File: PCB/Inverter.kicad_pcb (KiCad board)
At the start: 2 copper layers, 71.4 x 98.7 mm, 79 parts, among them J1 Conn_01x02, J2 Conn_01x05_Pin, J3 Conn_01x05_Pin, Q1 STP110N8F6, Q2 STP110N8F6, Q3 STP110N8F6, Q4 STP110N8F6, Q5 STP110N8F6, Q6 STP110N8F6, U1 XL7015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

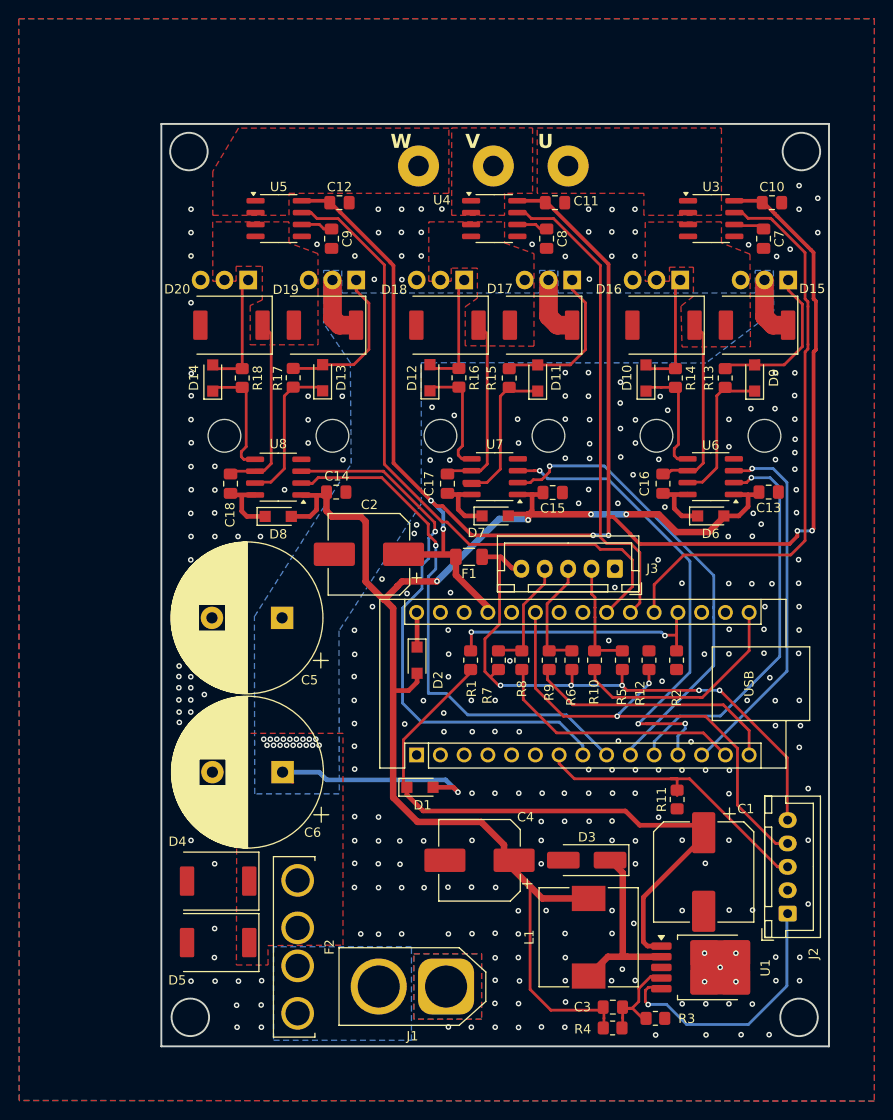
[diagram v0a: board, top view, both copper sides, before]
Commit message: Change#009
Changed the pin on phase W from 5 to 3 (so that all PWMs are at the same frequency);
Added a thermal barrier for all components on the negative side to make it easier to assemble the device;
Changed the size of the board, it became a little larger (to increase the ground current);
Added frames for connectors with a description in the diagram for a better understanding of which connector is for what.
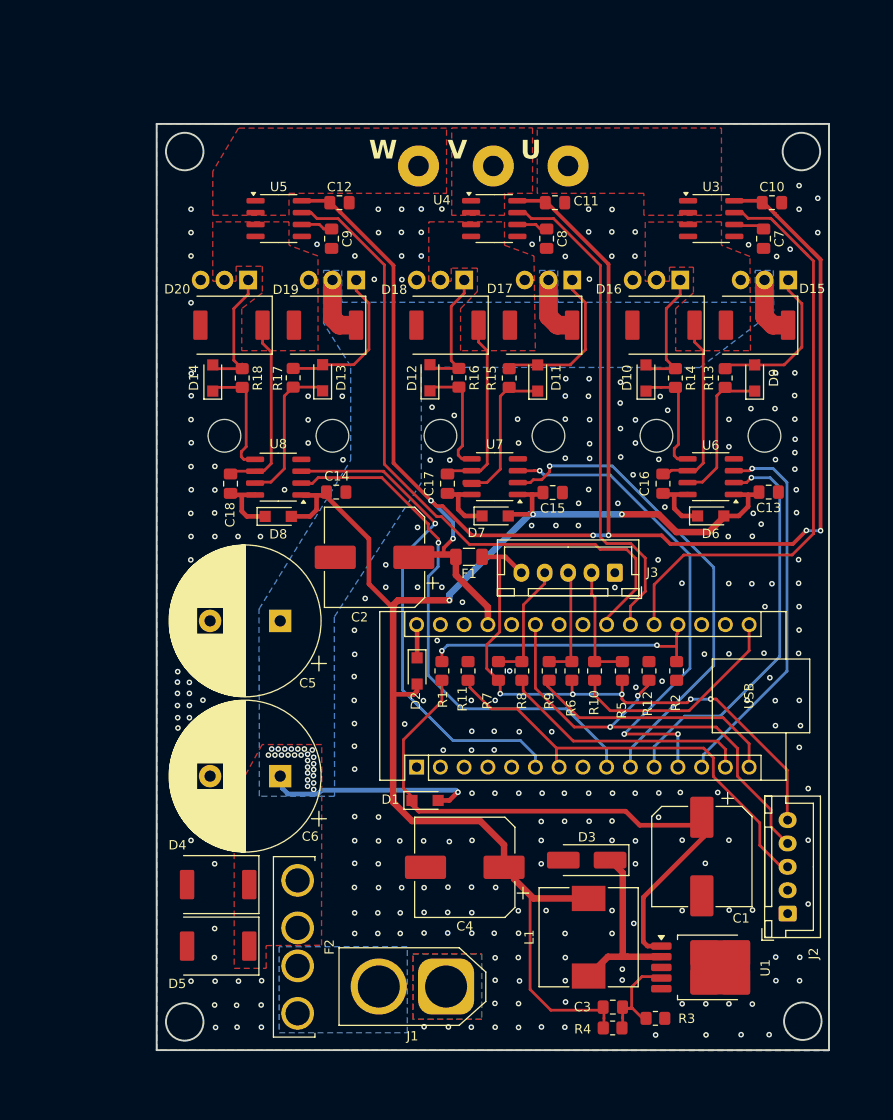
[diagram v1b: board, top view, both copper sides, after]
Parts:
- C1: value 220uF 63V -> 100uF 63V
- C2, C4: footprint Capacitor_SMD:CP_Elec_8x10.5 -> Capacitor_SMD:CP_Elec_10x10.5
- D15, D16, D17, D18, D19, D20, D4, D5: value SS56 -> SS510
- moved R11 26.2 mm to (137.1, 101.9), turned to -90 degrees
- moved R1 3.28 mm to (134.3, 101.9)
- moved C4 1.74 mm to (136.8, 122.9)
- moved C1 1.66 mm to (162.1, 121.7)
- moved D1 1.51 mm to (132.5, 115.7)
- moved A1 1.31 mm to (131.6, 112.2)
- moved D2 1.15 mm to (131.7, 101.9)
- moved R10 1.15 mm to (150.6, 101.9)
- moved R12 1.15 mm to (156.4, 101.9)
- moved R2 1.15 mm to (159.4, 101.9)
- moved R5 1.15 mm to (153.6, 101.9)
- moved R6 1.15 mm to (148.2, 101.9)
- moved R7 1.15 mm to (140.3, 101.9)
- moved R8 1.15 mm to (142.8, 101.9)
- moved R9 1.15 mm to (145.8, 101.9)
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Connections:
- A1 pad 6: unconnected-(A1-D3-Pad6) -> /PWM_W
- A1 pad 8: /PWM_W -> unconnected-(A1-D5-Pad8)
- J2 pad 1: /ON -> GND
- U1 pad 5: /ON -> unconnected-(U1-EN-Pad5)
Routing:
- net /ON: track 27.6 -> 0.00 mm, vias 1 -> 0
- net /CWR: track 32.3 -> 46.8 mm
- net /PWM_W: track 59.6 -> 54.3 mm
- net +5V: track 186.2 -> 189.6 mm
- net +10V: track 151.4 -> 149.1 mm, vias 4 -> 3
- net /Vbatt: track 28.4 -> 30.6 mm
- net /Cur_U: track 61.5 -> 63.4 mm
- net /Cur_W: track 70.0 -> 71.9 mm
- net /IN_V: track 49.8 -> 51.6 mm
- net /POT: track 51.8 -> 50.0 mm
- net /Cur_V: track 52.0 -> 53.8 mm
- net /PWM_V: track 51.8 -> 53.5 mm
- net /IN_U: track 41.7 -> 43.3 mm
- net +5V_Fuse: track 66.8 -> 65.3 mm
- net Net-(J3-Pin_2): track 11.8 -> 13.0 mm
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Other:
- board size 71.4 x 98.7 mm -> 71.9 x 99.1 mm
- board text added: "Battery: 8S VCC: 24,0..33,6V I(max): 20A V0.1"
- board text removed: "Battery: 8S VCC: 24,0..33,6V I(max): 20A"
